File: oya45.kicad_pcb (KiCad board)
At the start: 2 copper layers, 190.5 x 95.2 mm, 108 parts, among them U1 ProMicro

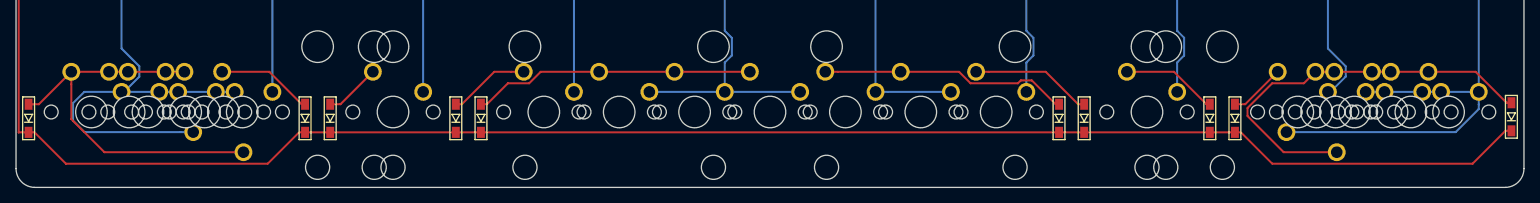
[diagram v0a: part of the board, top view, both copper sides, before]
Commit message: cleaned up switch position and tracks, and added gerbers
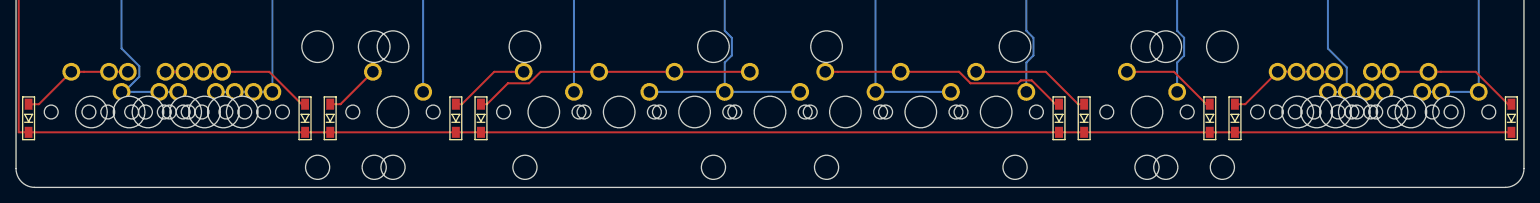
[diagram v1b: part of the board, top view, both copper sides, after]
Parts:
- moved D40 0.19 mm to (236.5, 115.1)
- turned MX51 to 180 degrees
- turned MX58 to 180 degrees
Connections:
- MX51 pad 1: col0 -> col1
- MX51 pad 2: Net-(D31-Pad2) -> Net-(D32-Pad2)
- MX52 pad 1: col0 -> col1
- MX52 pad 2: Net-(D31-Pad2) -> Net-(D32-Pad2)
- MX54 pad 1: col0 -> col1
- MX54 pad 2: Net-(D31-Pad2) -> Net-(D32-Pad2)
- MX57 pad 1: col9 -> col8
- MX57 pad 2: Net-(D40-Pad2) -> Net-(D39-Pad2)
- MX58 pad 1: col9 -> col8
- MX58 pad 2: Net-(D40-Pad2) -> Net-(D39-Pad2)
- MX60 pad 1: col9 -> col8
- MX60 pad 2: Net-(D40-Pad2) -> Net-(D39-Pad2)
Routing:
- net Net-(D31-Pad2): track 50.8 -> 14.2 mm
- net col9: track 216.9 -> 182.1 mm
- net col0: track 167.3 -> 135.4 mm
- net Net-(D40-Pad2): track 51.0 -> 19.3 mm
- net col1: track 109.7 -> 116.9 mm
- net Net-(D39-Pad2): track 7.10 -> 14.2 mm
- net Net-(D32-Pad2): track 12.2 -> 19.3 mm
- net row4: track 330.7 -> 324.0 mm
- net col8: track 161.1 -> 167.2 mm

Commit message: added ground fill
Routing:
- added copper zone on B.Cu, net (none)
- added copper zone on F.Cu, net (none)
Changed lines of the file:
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@@
   (segment (start 216.23974 28.91474) (end 133.01026 28.91474) (width 0.254) (layer B.Cu) (net 60))
   (segment (start 232.41 111.76) (end 225.26625 111.76) (width 0.254) (layer B.Cu) (net 60))
+  (zone (net 0) (net_name "") (layer F.Cu) (hatch edge 0.508)
+    (connect_pads (clearance 0.508))
+    (min_thickness 0.254)
+    (fill yes (arc_segments 32) (thermal_gap 0.508) (thermal_bridge_width 0.508))
+    (polygon
+      (pts
+        (xy 47.625 28.575) (xy 238.125 28.575) (xy 238.125 123.825) (xy 47.625 123.825)
+      )
+    )
+  )
+  (zone (net 0) (net_name "") (layer B.Cu) (hatch edge 0.508)
+    (connect_pads (clearance 0.508))
+    (min_thickness 0.254)
+    (fill yes (arc_segments 32) (thermal_gap 0.508) (thermal_bridge_width 0.508))
+    (polygon
+      (pts
+        (xy 47.625 28.575) (xy 238.125 28.575) (xy 238.125 123.825) (xy 47.625 123.825)
+      )
+    )
+  )
 )
